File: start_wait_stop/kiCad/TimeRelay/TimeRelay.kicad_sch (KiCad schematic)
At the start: 15 parts, among them J1 230V AC Input, J10 Relay, J2 230V AC Input, J3 Relay, J4 Relay, J5 230V AC OUTPUT, J6 230V AC OUTPUT, J7 Relay, J8 Relay, J9 Relay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

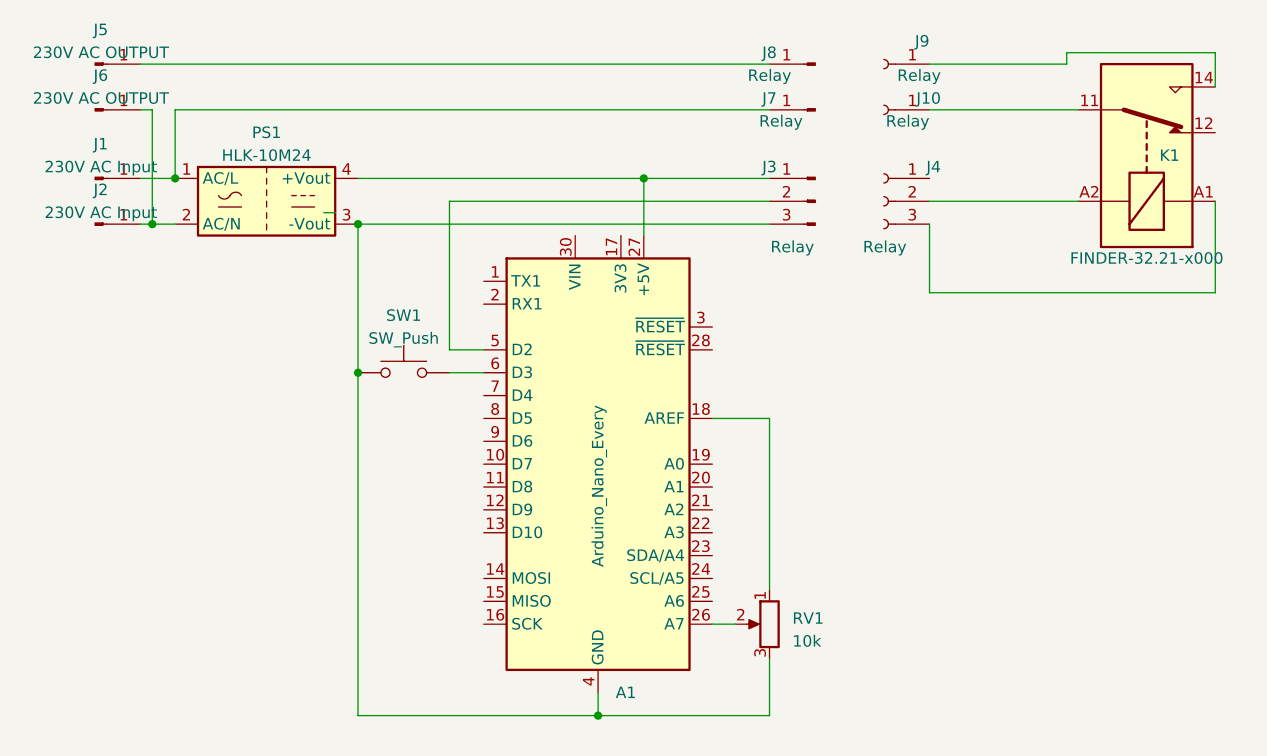
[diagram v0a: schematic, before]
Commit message: Fixed schematic issue
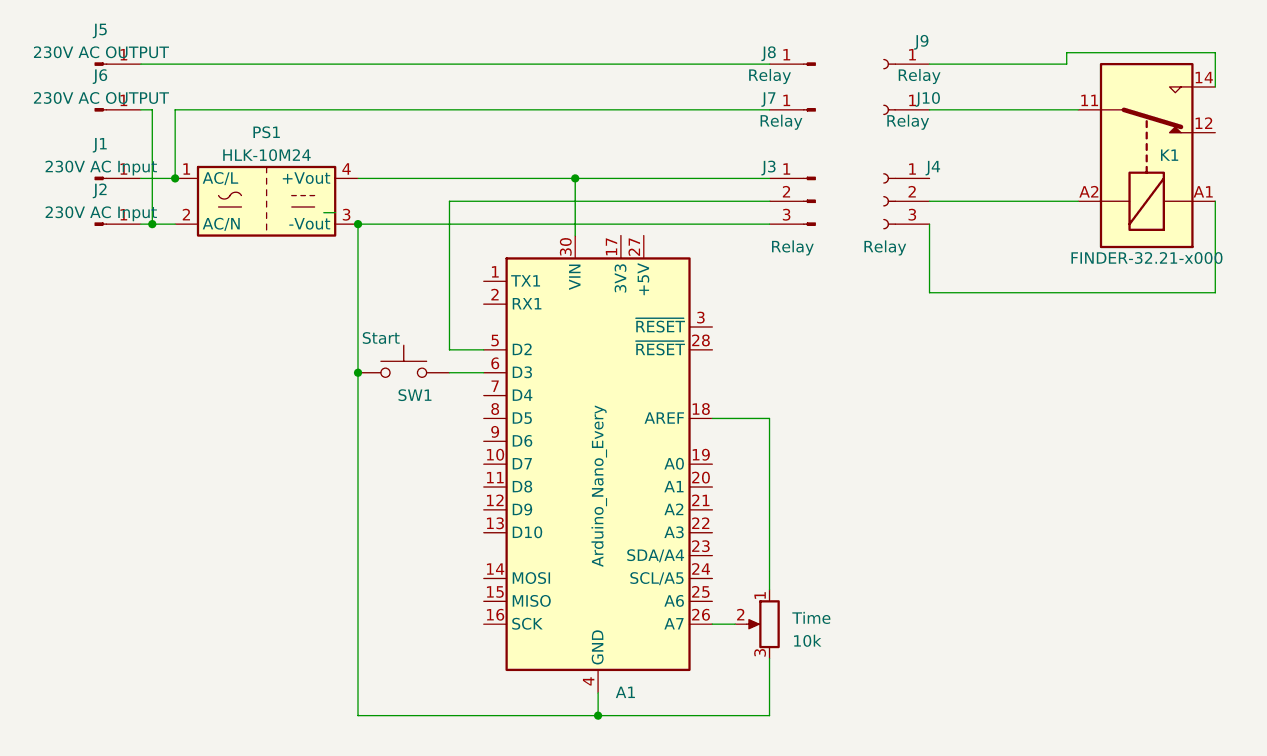
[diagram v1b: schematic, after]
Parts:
- SW1: value SW_Push -> Start
- renumbered RV1 to Time
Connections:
- net at J3.1 (Pin_1), PS1.4 (+Vout): now also A1.30 (VIN); no longer A1.27 (+5V)
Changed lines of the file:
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@@
   (junction (at 72.39 72.39) (diameter 0) (color 0 0 0 0)
   )
-  (junction (at 104.14 50.8) (diameter 0) (color 0 0 0 0)
-  )
   (junction (at 52.07 50.8) (diameter 0) (color 0 0 0 0)
   )
+  (junction (at 96.52 50.8) (diameter 0) (color 0 0 0 0)
+  )
   (wire (pts (xy 72.39 110.49) (xy 99.06 110.49))
     (stroke (width 0) (type default))
   )
+  (wire (pts (xy 96.52 50.8) (xy 96.52 57.15))
+    (stroke (width 0) (type default))
+  )
   (wire (pts (xy 49.53 43.18) (xy 49.53 55.88))
     (stroke (width 0) (type default))
@@
     (stroke (width 0) (type default))
   )
-  (wire (pts (xy 104.14 50.8) (xy 104.14 57.15))
-    (stroke (width 0) (type default))
-  )
   (wire (pts (xy 151.13 38.1) (xy 151.13 36.83))
     (stroke (width 0) (type default))
@@
     (stroke (width 0) (type default))
   )
-  (wire (pts (xy 104.14 50.8) (xy 118.11 50.8))
-    (stroke (width 0) (type default))
-  )
   (wire (pts (xy 48.26 38.1) (xy 118.11 38.1))
     (stroke (width 0) (type default))
@@
     (stroke (width 0) (type default))
   )
-  (wire (pts (xy 72.39 50.8) (xy 104.14 50.8))
+  (wire (pts (xy 72.39 50.8) (xy 96.52 50.8))
     (stroke (width 0) (type default))
   )
@@
   )
   (wire (pts (xy 82.55 53.34) (xy 82.55 69.85))
+    (stroke (width 0) (type default))
+  )
+  (wire (pts (xy 96.52 50.8) (xy 118.11 50.8))
     (stroke (width 0) (type default))
   )
@@
   (symbol (lib_id "Device:R_Potentiometer") (at 118.11 100.33 0) (mirror y) (unit 1)
     (in_bom yes) (on_board yes) (dnp no)
-    (property "Reference" "RV1" (at 120.65 99.695 0)
+    (property "Reference" "Time" (at 120.65 99.695 0)
       (effects (font (size 1.27 1.27)) (justify right))
     )
@@
       (project "TimeRelay"
         (path "/e63dc5b1-1efa-4968-8eca-c664ae4ae638"
-          (reference "RV1") (unit 1)
+          (reference "Time") (unit 1)
         )
       )
@@
   )
   (symbol (lib_id "Switch:SW_Push") (at 77.47 72.39 0) (unit 1)
-    (in_bom yes) (on_board yes) (dnp no) (fields_autoplaced)
-    (property "Reference" "SW1" (at 77.47 66.04 0)
-      (effects (font (size 1.27 1.27)))
-    )
-    (property "Value" "SW_Push" (at 77.47 68.58 0)
-      (effects (font (size 1.27 1.27)))
-    )
+    (in_bom yes) (on_board yes) (dnp no)
+    (property "Reference" "SW1" (at 78.74 74.93 0)
+      (effects (font (size 1.27 1.27)))
+    )
+    (property "Value" "Start" (at 74.93 68.58 0)
+      (effects (font (size 1.27 1.27)))
+    )

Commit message: Playing arround witj KiCAD.
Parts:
- removed J1, J2: 230V AC Input, symbol Connector:Conn_01x01_Pin
- removed J10, J9: Relay, symbol Connector:Conn_01x01_Socket
- removed J3: Relay, symbol Connector:Conn_01x03_Pin
- removed J4: Relay, symbol Connector:Conn_01x03_Socket
- removed J5, J6: 230V AC OUTPUT, symbol Connector:Conn_01x01_Pin
- removed J7, J8: Relay, symbol Connector:Conn_01x01_Pin
- added J1: 230V Input, Connector_Wire:SolderWire-1.5sqmm_1x02_P7.8mm_D1.7mm_OD3.9mm, symbol Connector:Conn_01x02_Socket
- added J10: Relay command, Connector_PinSocket_2.54mm:PinSocket_1x03_P2.54mm_Vertical, symbol Connector:Conn_01x03_Socket
- added J13: Relay, Connector_PinSocket_2.54mm:PinSocket_1x03_P2.54mm_Vertical, symbol Connector:Conn_01x03_Socket
- added J2: 230V Output, Connector_Wire:SolderWire-1.5sqmm_1x02_P7.8mm_D1.7mm_OD3.9mm, symbol Connector:Conn_01x02_Socket
- added J3: Relay NO contact, Connector_Wire:SolderWire-1.5sqmm_1x02_P7.8mm_D1.7mm_OD3.9mm, symbol Connector:Conn_01x02_Socket
- added J4: Conn_01x02_Socket, Connector_Wire:SolderWire-1.5sqmm_1x02_P7.8mm_D1.7mm_OD3.9mm, symbol Connector:Conn_01x02_Socket
- K1: value FINDER-32.21-x000 -> 5V Relay Module
- SW1: footprint (none) -> Button_Switch_THT:SW_Tactile_SPST_Angled_PTS645Vx83-2LFS
- Time1: renamed from Time; footprint (none) -> Potentiometer_THT:Potentiometer_Alps_RK09L_Single_Vertical
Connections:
- net at K1.14: now also J4.2 (Pin_2)
- net at PS1.1 (AC/L): now also J1.1 (Pin_1), J3.2 (Pin_2)
- net at PS1.2 (AC/N): now also J1.2 (Pin_2), J2.2 (Pin_2)
- net GND: now reaches A1.29 (GND), A1.4 (GND), PS1.3 (-Vout), SW1.1, Time1.3
- net GND: now also J10.3 (Pin_3)
- net at A1.30 (VIN), PS1.4 (+Vout): now also J10.1 (Pin_1)
- net at A1.5 (D2): now also J10.2 (Pin_2)
- net at K1.A2: now also J13.2 (Pin_2)
- net at K1.A1: now also J13.3 (Pin_3)
- net at K1.11: now also J4.1 (Pin_1)
- new net: J2.1 (Pin_1), J3.1 (Pin_1)
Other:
- moved on the sheet: A1, K1, Time1
